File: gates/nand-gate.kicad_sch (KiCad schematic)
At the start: 5 parts, among them Q7 NPN, Q8 NPN

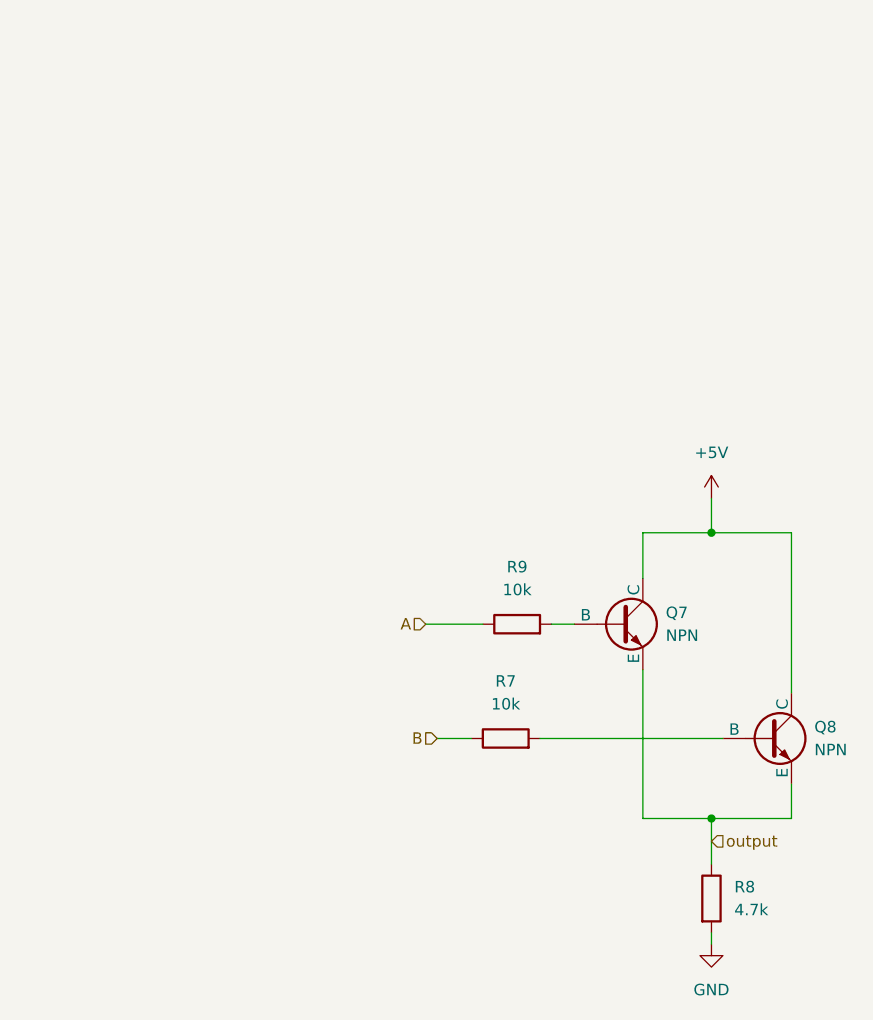
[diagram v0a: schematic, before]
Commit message: Improved logic gates
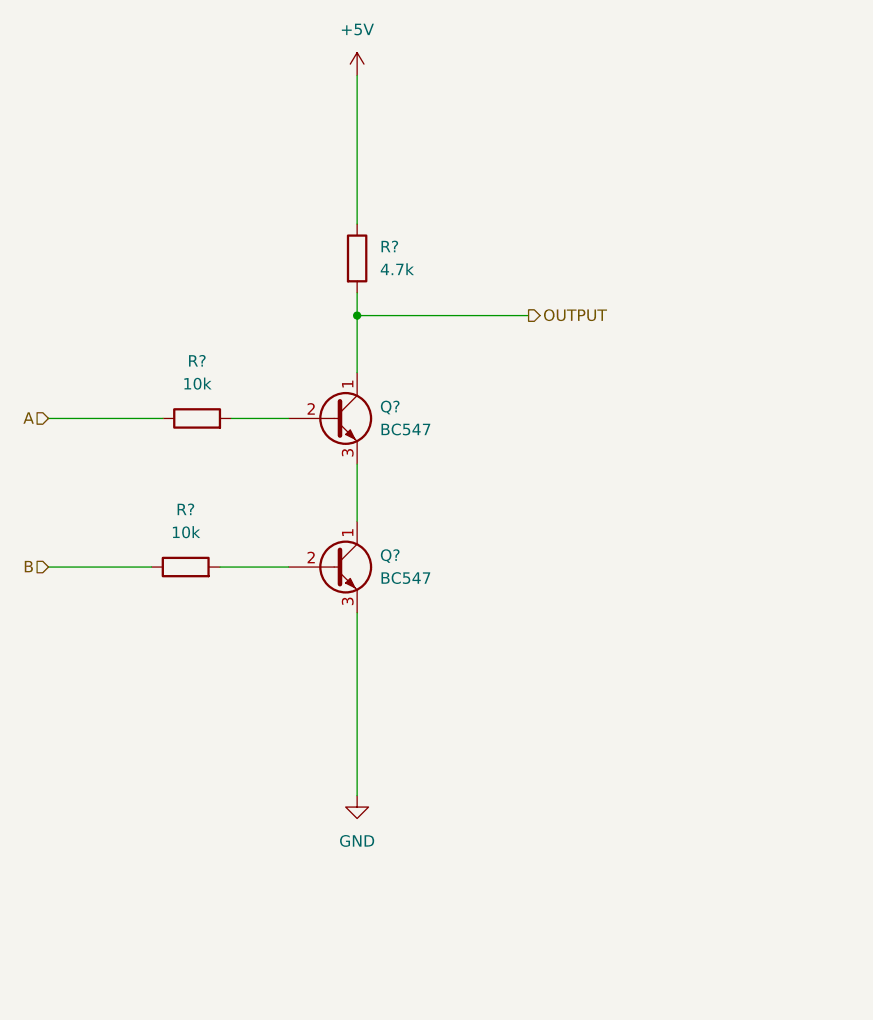
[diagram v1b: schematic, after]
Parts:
- removed Q7, Q8: NPN, symbol Simulation_SPICE:NPN
- removed R7, R9: 10k, symbol Device:R
- removed R8: 4.7k, symbol Device:R
- added Q? (x2): BC547, Package_TO_SOT_THT:TO-92_Inline, symbol Transistor_BJT:BC547
- added R? (x2): 10k, Resistor_SMD:R_0201_0603Metric, symbol Device:R
- added R?: 4.7k, Resistor_SMD:R_0201_0603Metric, symbol Device:R
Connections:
- net +5V: now also R?.1
- net A: now also R?.1
- net B: now also R?.1
- net GND: now also Q?.3 (E)
- new net: Q?.2 (B), R?.2 (x2)
- new net: Q?.1 (C), Q?.3 (E)
- new net OUTPUT: Q?.1 (C), R?.2

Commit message: replaced circuitry in half adder with reusable gates
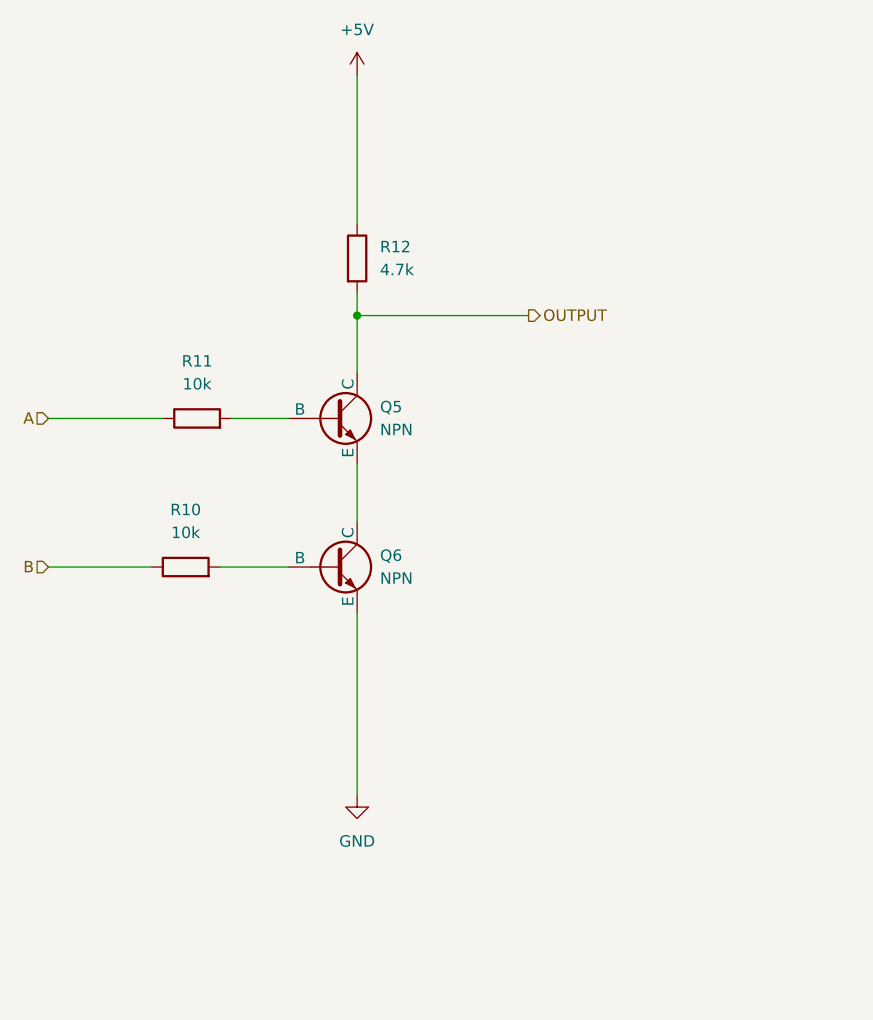
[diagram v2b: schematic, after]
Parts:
- removed Q? (x2): BC547, Package_TO_SOT_THT:TO-92_Inline, symbol Transistor_BJT:BC547
- added Q5, Q6: NPN, symbol Simulation_SPICE:NPN
- gave numbers to parts that had none: 3
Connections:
- net GND: now also Q6.3 (E)
- net OUTPUT: now also Q5.1 (C)
- net at R11.2: now also Q5.2 (B)
- net at R10.2: now also Q6.2 (B)
- new net: Q5.3 (E), Q6.1 (C)

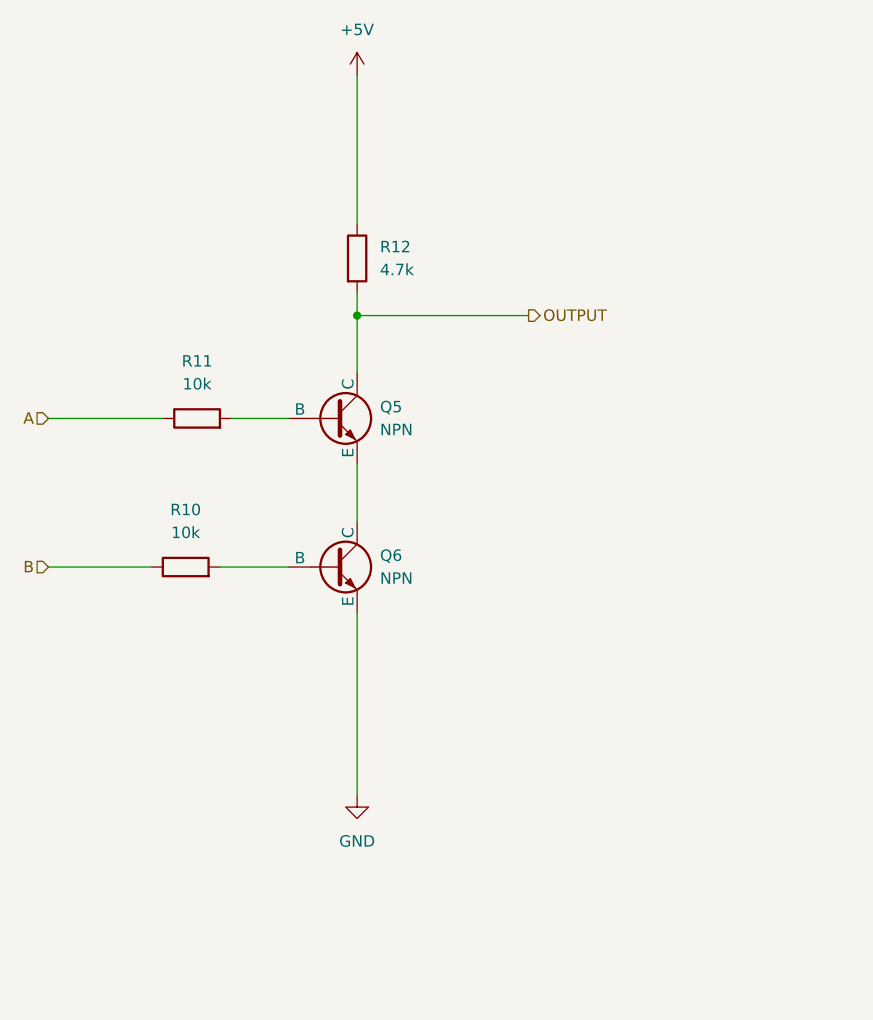
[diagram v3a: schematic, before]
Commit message: Fixed gates and moved half adder to its own directory
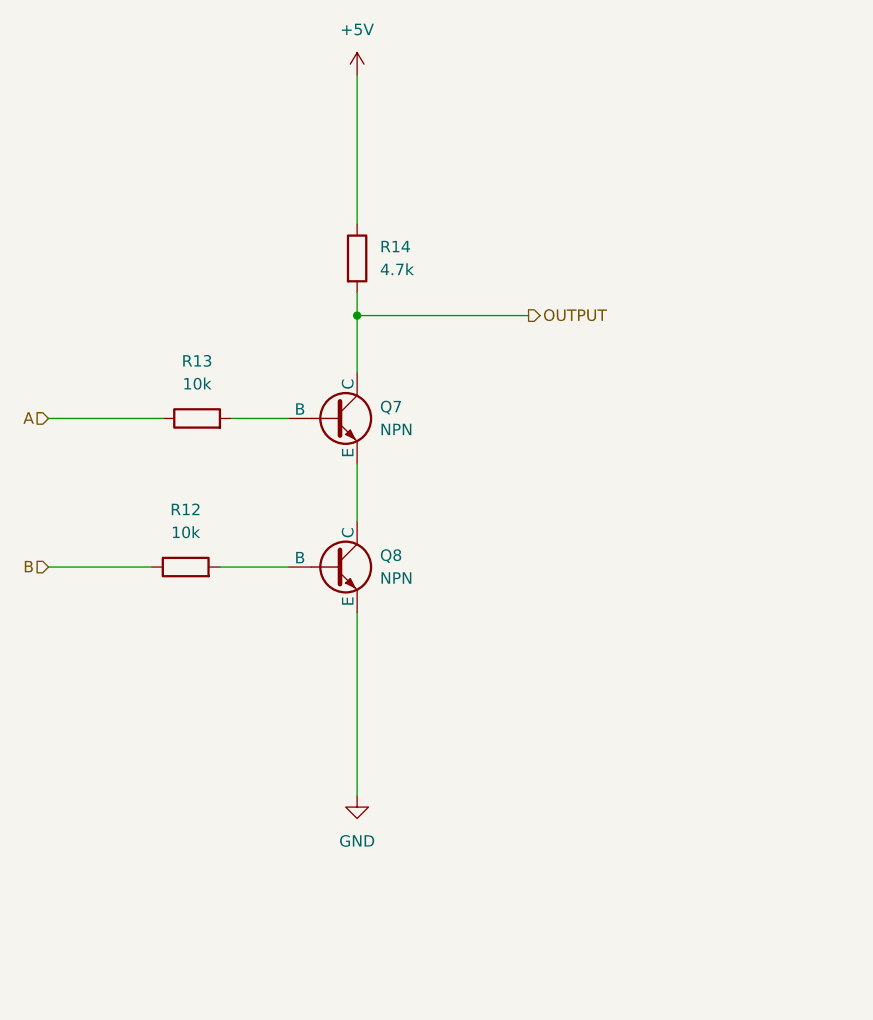
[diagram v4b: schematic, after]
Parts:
- renumbered Q5 to Q7, Q6 to Q8, R10 to R12, R11 to R13, R12 to R14
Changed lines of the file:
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@@
 		(dnp no)
 		(fields_autoplaced yes)
-		(property "Reference" "Q5"
+		(property "Reference" "Q7"
 			(at 97.79 77.4699 0)
 			(effects
@@
 		)
 		(instances
-			(project ""
-				(path "/88c27409-0a88-4cf1-8b65-cf7271709e32/9ae6b3ee-29f0-4a20-9e44-32b28e8d9225/3c6c3515-201d-4b02-b79f-e9c4c0dfa7c4"
-					(reference "Q5")
-					(unit 1)
-				)
-				(path "/88c27409-0a88-4cf1-8b65-cf7271709e32/c6fa08ba-c5fb-43d8-850f-3e5322725fc3/3c6c3515-201d-4b02-b79f-e9c4c0dfa7c4"
-					(reference "Q9")
+			(project "half-adder"
+				(path "/88c27409-0a88-4cf1-8b65-cf7271709e32/9ae6b3ee-29f0-4a20-9e44-32b28e8d9225/3c6c3515-201d-4b02-b79f-e9c4c0dfa7c4"
+					(reference "Q7")
+					(unit 1)
+				)
+				(path "/88c27409-0a88-4cf1-8b65-cf7271709e32/c6fa08ba-c5fb-43d8-850f-3e5322725fc3/3c6c3515-201d-4b02-b79f-e9c4c0dfa7c4"
+					(reference "Q12")
 					(unit 1)
 				)
@@
 		(dnp no)
 		(fields_autoplaced yes)
-		(property "Reference" "R11"
+		(property "Reference" "R13"
 			(at 77.47 72.39 90)
 			(effects
@@
 			(project "half-adder"
 				(path "/88c27409-0a88-4cf1-8b65-cf7271709e32/9ae6b3ee-29f0-4a20-9e44-32b28e8d9225/3c6c3515-201d-4b02-b79f-e9c4c0dfa7c4"
-					(reference "R11")
-					(unit 1)
-				)
-				(path "/88c27409-0a88-4cf1-8b65-cf7271709e32/c6fa08ba-c5fb-43d8-850f-3e5322725fc3/3c6c3515-201d-4b02-b79f-e9c4c0dfa7c4"
-					(reference "R17")
-					(unit 1)
-				)
-			)
-			(project "half-adder"
-				(path "/aa2ffd02-03c7-43f5-905d-233d00be0633/8e657cf9-09ea-4d19-97ba-111b741f01c5/3c6c3515-201d-4b02-b79f-e9c4c0dfa7c4"
-					(reference "R11")
+					(reference "R13")
+					(unit 1)
+				)
+				(path "/88c27409-0a88-4cf1-8b65-cf7271709e32/c6fa08ba-c5fb-43d8-850f-3e5322725fc3/3c6c3515-201d-4b02-b79f-e9c4c0dfa7c4"
+					(reference "R20")
 					(unit 1)
 				)
@@
 		(dnp no)
 		(fields_autoplaced yes)
-		(property "Reference" "R10"
+		(property "Reference" "R12"
 			(at 76.2 88.9 90)
 			(effects
@@
 			(project "half-adder"
 				(path "/88c27409-0a88-4cf1-8b65-cf7271709e32/9ae6b3ee-29f0-4a20-9e44-32b28e8d9225/3c6c3515-201d-4b02-b79f-e9c4c0dfa7c4"
-					(reference "R10")
-					(unit 1)
-				)
-				(path "/88c27409-0a88-4cf1-8b65-cf7271709e32/c6fa08ba-c5fb-43d8-850f-3e5322725fc3/3c6c3515-201d-4b02-b79f-e9c4c0dfa7c4"
-					(reference "R16")
-					(unit 1)
-				)
-			)
-			(project "half-adder"
-				(path "/aa2ffd02-03c7-43f5-905d-233d00be0633/8e657cf9-09ea-4d19-97ba-111b741f01c5/3c6c3515-201d-4b02-b79f-e9c4c0dfa7c4"
-					(reference "R10")
+					(reference "R12")
+					(unit 1)
+				)
+				(path "/88c27409-0a88-4cf1-8b65-cf7271709e32/c6fa08ba-c5fb-43d8-850f-3e5322725fc3/3c6c3515-201d-4b02-b79f-e9c4c0dfa7c4"
+					(reference "R19")
 					(unit 1)
 				)
@@
 		(dnp no)
 		(fields_autoplaced yes)
-		(property "Reference" "#PWR020"
+		(property "Reference" "#PWR024"
 			(at 95.25 127 0)
 			(effects
@@
 			(project "half-adder"
 				(path "/88c27409-0a88-4cf1-8b65-cf7271709e32/9ae6b3ee-29f0-4a20-9e44-32b28e8d9225/3c6c3515-201d-4b02-b79f-e9c4c0dfa7c4"
-					(reference "#PWR020")
-					(unit 1)
-				)
-				(path "/88c27409-0a88-4cf1-8b65-cf7271709e32/c6fa08ba-c5fb-43d8-850f-3e5322725fc3/3c6c3515-201d-4b02-b79f-e9c4c0dfa7c4"
 					(reference "#PWR024")
 					(unit 1)
 				)
-			)
-			(project "half-adder"
-				(path "/aa2ffd02-03c7-43f5-905d-233d00be0633/8e657cf9-09ea-4d19-97ba-111b741f01c5/3c6c3515-201d-4b02-b79f-e9c4c0dfa7c4"
-					(reference "#PWR020")
+				(path "/88c27409-0a88-4cf1-8b65-cf7271709e32/c6fa08ba-c5fb-43d8-850f-3e5322725fc3/3c6c3515-201d-4b02-b79f-e9c4c0dfa7c4"
+					(reference "#PWR030")
 					(unit 1)
 				)
@@
 		(dnp no)
 		(fields_autoplaced yes)
-		(property "Reference" "#PWR019"
+		(property "Reference" "#PWR023"
 			(at 95.25 44.45 0)
 			(effects
@@
 			(project "half-adder"
 				(path "/88c27409-0a88-4cf1-8b65-cf7271709e32/9ae6b3ee-29f0-4a20-9e44-32b28e8d9225/3c6c3515-201d-4b02-b79f-e9c4c0dfa7c4"
-					(reference "#PWR019")
-					(unit 1)
-				)
-				(path "/88c27409-0a88-4cf1-8b65-cf7271709e32/c6fa08ba-c5fb-43d8-850f-3e5322725fc3/3c6c3515-201d-4b02-b79f-e9c4c0dfa7c4"
 					(reference "#PWR023")
 					(unit 1)
 				)
-			)
-			(project "half-adder"
-				(path "/aa2ffd02-03c7-43f5-905d-233d00be0633/8e657cf9-09ea-4d19-97ba-111b741f01c5/3c6c3515-201d-4b02-b79f-e9c4c0dfa7c4"
-					(reference "#PWR019")
+				(path "/88c27409-0a88-4cf1-8b65-cf7271709e32/c6fa08ba-c5fb-43d8-850f-3e5322725fc3/3c6c3515-201d-4b02-b79f-e9c4c0dfa7c4"
+					(reference "#PWR029")
 					(unit 1)
 				)
@@
 		(dnp no)
 		(fields_autoplaced yes)
-		(property "Reference" "R12"
+		(property "Reference" "R14"
 			(at 97.79 59.6899 0)
 			(effects
@@
 			(project "half-adder"
 				(path "/88c27409-0a88-4cf1-8b65-cf7271709e32/9ae6b3ee-29f0-4a20-9e44-32b28e8d9225/3c6c3515-201d-4b02-b79f-e9c4c0dfa7c4"
-					(reference "R12")
-					(unit 1)
-				)
-				(path "/88c27409-0a88-4cf1-8b65-cf7271709e32/c6fa08ba-c5fb-43d8-850f-3e5322725fc3/3c6c3515-201d-4b02-b79f-e9c4c0dfa7c4"
-					(reference "R18")
-					(unit 1)
-				)
-			)
-			(project "half-adder"
-				(path "/aa2ffd02-03c7-43f5-905d-233d00be0633/8e657cf9-09ea-4d19-97ba-111b741f01c5/3c6c3515-201d-4b02-b79f-e9c4c0dfa7c4"
-					(reference "R12")
+					(reference "R14")
+					(unit 1)
+				)
+				(path "/88c27409-0a88-4cf1-8b65-cf7271709e32/c6fa08ba-c5fb-43d8-850f-3e5322725fc3/3c6c3515-201d-4b02-b79f-e9c4c0dfa7c4"
+					(reference "R21")
 					(unit 1)
 				)
@@
 		(dnp no)
 		(fields_autoplaced yes)
-		(property "Reference" "Q6"
+		(property "Reference" "Q8"
 			(at 97.79 93.9799 0)
 			(effects
@@
 		)
 		(instances
-			(project ""
-				(path "/88c27409-0a88-4cf1-8b65-cf7271709e32/9ae6b3ee-29f0-4a20-9e44-32b28e8d9225/3c6c3515-201d-4b02-b79f-e9c4c0dfa7c4"
-					(reference "Q6")
-					(unit 1)
-				)
-				(path "/88c27409-0a88-4cf1-8b65-cf7271709e32/c6fa08ba-c5fb-43d8-850f-3e5322725fc3/3c6c3515-201d-4b02-b79f-e9c4c0dfa7c4"
-					(reference "Q10")
-					(unit 1)
-				)
+			(project "half-adder"
+				(path "/88c27409-0a88-4cf1-8b65-cf7271709e32/9ae6b3ee-29f0-4a20-9e44-32b28e8d9225/3c6c3515-201d-4b02-b79f-e9c4c0dfa7c4"
+					(reference "Q8")
+					(unit 1)
+				)
+				(path "/88c27409-0a88-4cf1-8b65-cf7271709e32/c6fa08ba-c5fb-43d8-850f-3e5322725fc3/3c6c3515-201d-4b02-b79f-e9c4c0dfa7c4"
+					(reference "Q13")
+					(unit 1)
+				)
